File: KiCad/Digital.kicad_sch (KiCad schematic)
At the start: 33 parts, among them IC1 PIC24H, J2 DE9_Plug_MountingHoles, J3 DE9_Plug_MountingHoles, J4 Conn_01x03, J7 Conn_01x05, SW1 SW_DP3T, SW2 SW_DP3T, SW3 SW_DP3T, SW4 OP/CL, SW7 OP/CL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

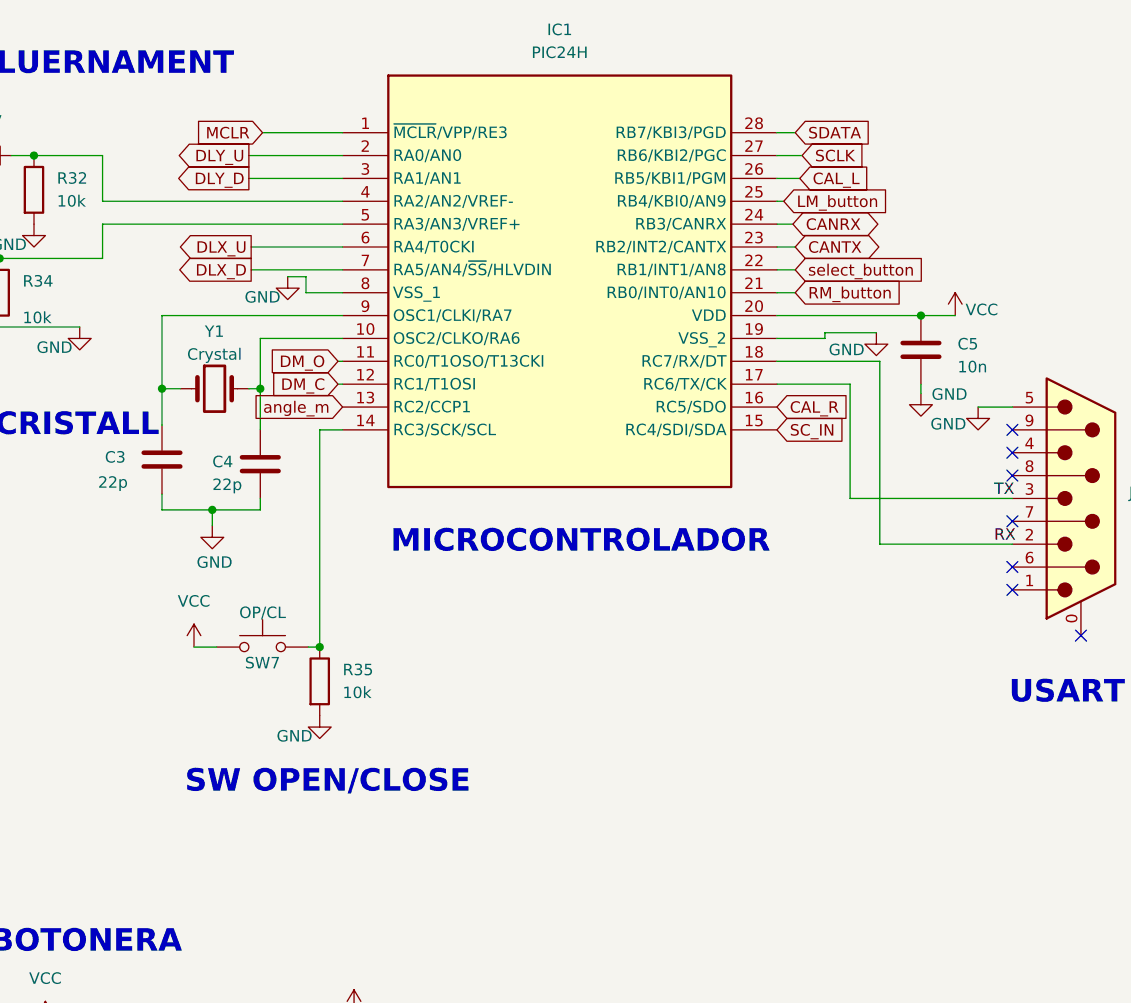
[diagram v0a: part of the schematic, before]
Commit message: afegit esquematic (testpoints + extensor de pines) falta acabar placement
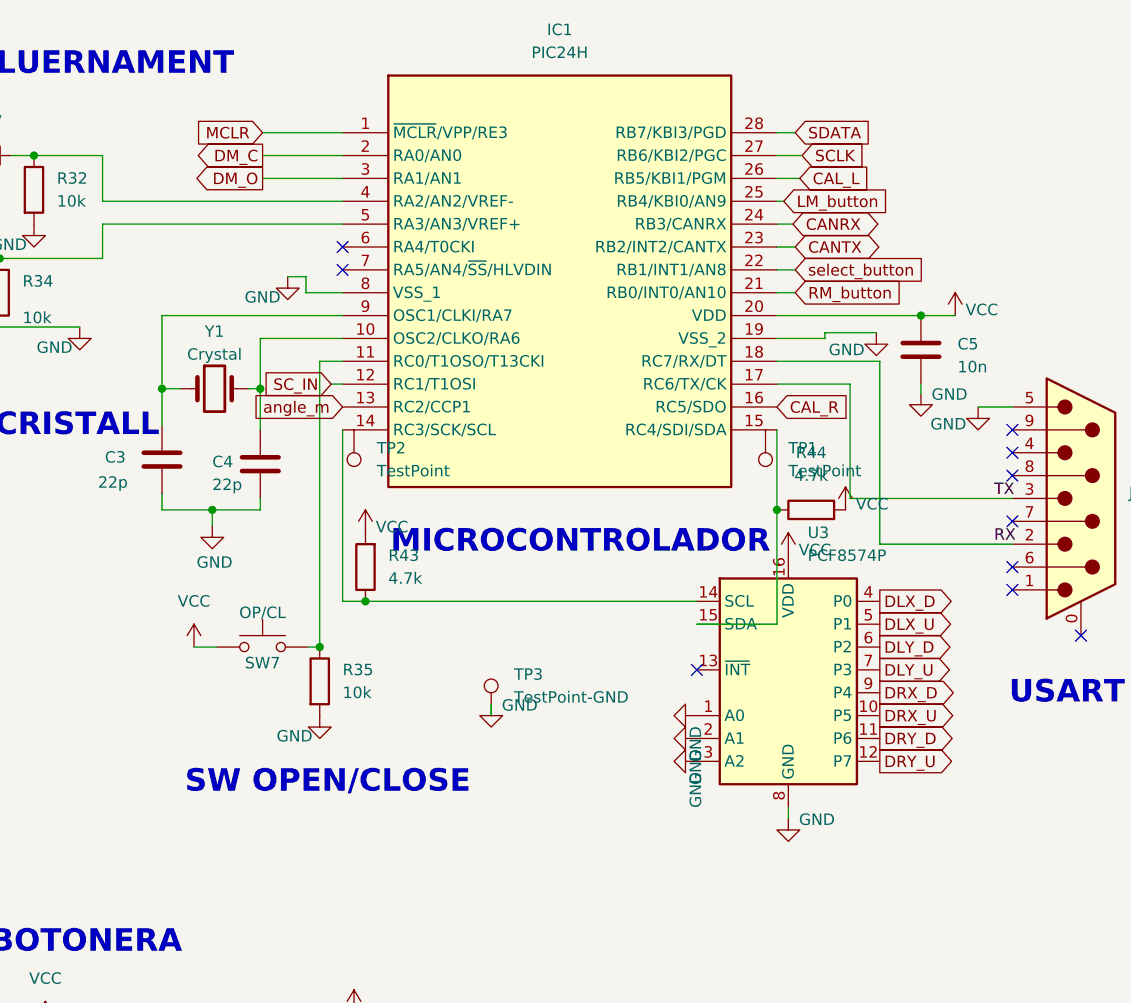
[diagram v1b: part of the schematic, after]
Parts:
- added R43, R44: 4.7k, Resistor_SMD:R_1206_3216Metric_Pad1.30x1.75mm_HandSolder, symbol Device:R
- added TP1, TP2: TestPoint, TestPoint:TestPoint_THTPad_D1.5mm_Drill0.7mm, symbol Connector:TestPoint
- added TP3: TestPoint-GND, TestPoint:TestPoint_THTPad_D1.5mm_Drill0.7mm, symbol Connector:TestPoint
- added U3: PCF8574P, Package_DIP:DIP-16_W7.62mm, symbol Interface_Expansion:PCF8574P
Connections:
- net DLX_D: now also U3.4 (P0); no longer IC1.7 (RA5/AN4/~{SS}/HLVDIN)
- net DLX_U: now also U3.5 (P1); no longer IC1.6 (RA4/T0CKI)
- net DLY_D: now also U3.6 (P2); no longer IC1.3 (RA1/AN1)
- net DLY_U: now also U3.7 (P3); no longer IC1.2 (RA0/AN0)
- net DM_C: now also IC1.2 (RA0/AN0); no longer IC1.12 (RC1/T1OSI)
- net DM_O: now also IC1.3 (RA1/AN1); no longer IC1.11 (RC0/T1OSO/T13CKI)
- net GND: now also TP3.1, U3.1 (A0), U3.2 (A1), U3.3 (A2), U3.8 (GND)
- net SC_IN: now also IC1.12 (RC1/T1OSI); no longer IC1.15 (RC4/SDI/SDA)
- net VCC: now also R43.2, R44.2, U3.16 (VDD)
- net at R35.1, SW7.2: now also IC1.11 (RC0/T1OSO/T13CKI); no longer IC1.14 (RC3/SCK/SCL)
- new net: IC1.14 (RC3/SCK/SCL), R43.1, U3.14 (SCL)
- new net: IC1.15 (RC4/SDI/SDA), R44.1, U3.15 (SDA)
- new net DRX_D: U3.9 (P4)
- new net DRX_U: U3.10 (P5)
- new net DRY_D: U3.11 (P6)
- new net DRY_U: U3.12 (P7)
- no-connect marks 15 -> 18

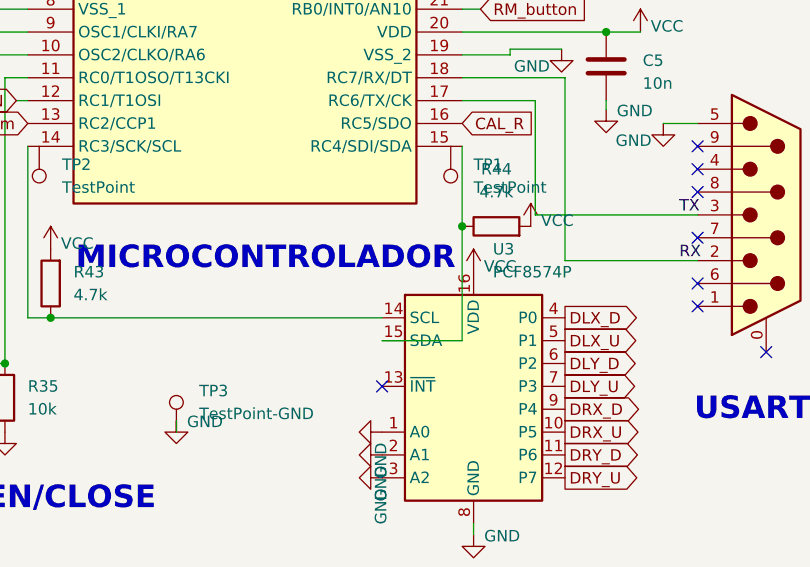
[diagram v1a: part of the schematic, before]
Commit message: canvis placement, afegir els r4emplazos que hi han a la pcb
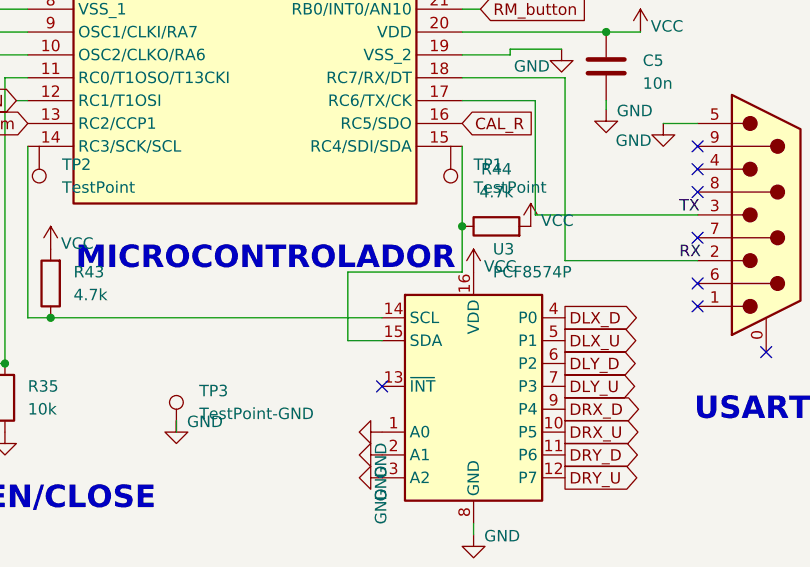
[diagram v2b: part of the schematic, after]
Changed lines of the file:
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@@
+	)
+	(junction
+		(at 132.08 69.85)
+		(diameter 0)
+		(color 0 0 0 0)
 	)
 	(junction
@@
 	)
 	(junction
-		(at 132.08 69.85)
-		(diameter 0)
-		(color 0 0 0 0)
-	)
-	(junction
 		(at 29.21 138.43)
 		(diameter 0)
@@
 	(wire
 		(pts
+			(xy 132.08 74.93) (xy 119.38 74.93)
+		)
+		(stroke
+			(width 0)
+			(type default)
+		)
+	)
+	(wire
+		(pts
+			(xy 119.38 74.93) (xy 119.38 82.55)
+		)
+		(stroke
+			(width 0)
+			(type default)
+		)
+	)
+	(wire
+		(pts
 			(xy 236.474 41.656) (xy 230.378 41.656)
 		)
@@
 	(wire
 		(pts
+			(xy 132.08 69.85) (xy 132.08 74.93)
+		)
+		(stroke
+			(width 0)
+			(type default)
+		)
+	)
+	(wire
+		(pts
 			(xy 198.882 35.56) (xy 201.93 35.56)
 		)
@@
 	(wire
 		(pts
+			(xy 119.38 82.55) (xy 123.19 82.55)
+		)
+		(stroke
+			(width 0)
+			(type default)
+		)
+	)
+	(wire
+		(pts
 			(xy 91.44 135.89) (xy 91.44 134.62)
 		)
@@
 	(wire
 		(pts
-			(xy 123.19 82.55) (xy 132.08 82.55)
-		)
-		(stroke
-			(width 0)
-			(type default)
-		)
-	)
-	(wire
-		(pts
 			(xy 40.64 144.78) (xy 50.8 144.78)
 		)
@@
 		)
 		(stroke
-			(width 0)
-			(type default)
-		)
-	)
-	(wire
-		(pts
-			(xy 132.08 82.55) (xy 132.08 69.85)
-		)
-		(stroke

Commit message: correcions de pcb
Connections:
- net CAL_L: now also IC1.2 (RA0/AN0); no longer IC1.26 (RB5/KBI1/PGM)
- net CAL_R: now also IC1.3 (RA1/AN1); no longer IC1.16 (RC5/SDO)
- net DLX_D: now also U3.9 (P4); no longer U3.4 (P0)
- net DLX_U: now also U3.10 (P5); no longer U3.5 (P1)
- net DLY_D: now also U3.4 (P0); no longer U3.6 (P2)
- net DLY_U: now also U3.5 (P1); no longer U3.7 (P3)
- net DM_C: now also U3.7 (P3); no longer IC1.2 (RA0/AN0)
- net DM_O: now also U3.6 (P2); no longer IC1.3 (RA1/AN1)
- net DRX_D: now also U3.11 (P6); no longer U3.9 (P4)
- net DRX_U: now also U3.12 (P7); no longer U3.10 (P5)
- net DRY_D: now also IC1.6 (RA4/T0CKI); no longer U3.11 (P6)
- net DRY_U: now also IC1.7 (RA5/AN4/~{SS}/HLVDIN); no longer U3.12 (P7)
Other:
- moved on the sheet: R31, R32, R33, R34

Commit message: pcb Tota connectada
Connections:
- net DLX_D: now also U3.12 (P7); no longer U3.9 (P4)
- net DRX_U: now also U3.9 (P4); no longer U3.12 (P7)
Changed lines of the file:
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@@
+		)
+	)
+	(global_label "DRX_U"
+		(shape output)
+		(at 143.51 90.17 0)
+		(fields_autoplaced yes)
+		(effects
+			(font
+				(size 1.27 1.27)
+			)
+			(justify left)
+		)
+		(property "Intersheetrefs" "${INTERSHEET_REFS}"
+			(at 152.5428 90.17 0)
+			(effects
+				(font
+					(size 1.27 1.27)
+				)
+				(justify left)
+				(hide yes)
+			)
 		)
 	)
@@
 		)
 	)
+	(global_label "DLX_D"
+		(shape output)
+		(at 143.51 97.79 0)
+		(fields_autoplaced yes)
+		(effects
+			(font
+				(size 1.27 1.27)
+			)
+			(justify left)
+		)
+		(property "Intersheetrefs" "${INTERSHEET_REFS}"
+			(at 152.2404 97.79 0)
+			(effects
+				(font
+					(size 1.27 1.27)
+				)
+				(justify left)
+				(hide yes)
+			)
+		)
+	)
 	(global_label "CAL_L"
 		(shape input)
@@
 		)
 	)
-	(global_label "DLX_D"
-		(shape output)
-		(at 143.51 90.17 0)
-		(fields_autoplaced yes)
-		(effects
-			(font
-				(size 1.27 1.27)
-			)
-			(justify left)
-		)
-		(property "Intersheetrefs" "${INTERSHEET_REFS}"
-			(at 152.2404 90.17 0)
-			(effects
-				(font
-					(size 1.27 1.27)
-				)
-				(justify left)
-				(hide yes)
-			)
-		)
-	)
 	(global_label "DRY_D"
 		(shape output)
@@
 			(effects
 				(font
-					(size 1.27 1.27)
-				)
-				(justify left)
-				(hide yes)
-			)
-		)
-	)
-	(global_label "DRX_U"
-		(shape output)
-		(at 143.51 97.79 0)
-		(fields_autoplaced yes)
-		(effects
-			(font
-				(size 1.27 1.27)
-			)
-			(justify left)
-		)
-		(property "Intersheetrefs" "${INTERSHEET_REFS}"
-			(at 152.5428 97.79 0)
-			(effects
-				(font

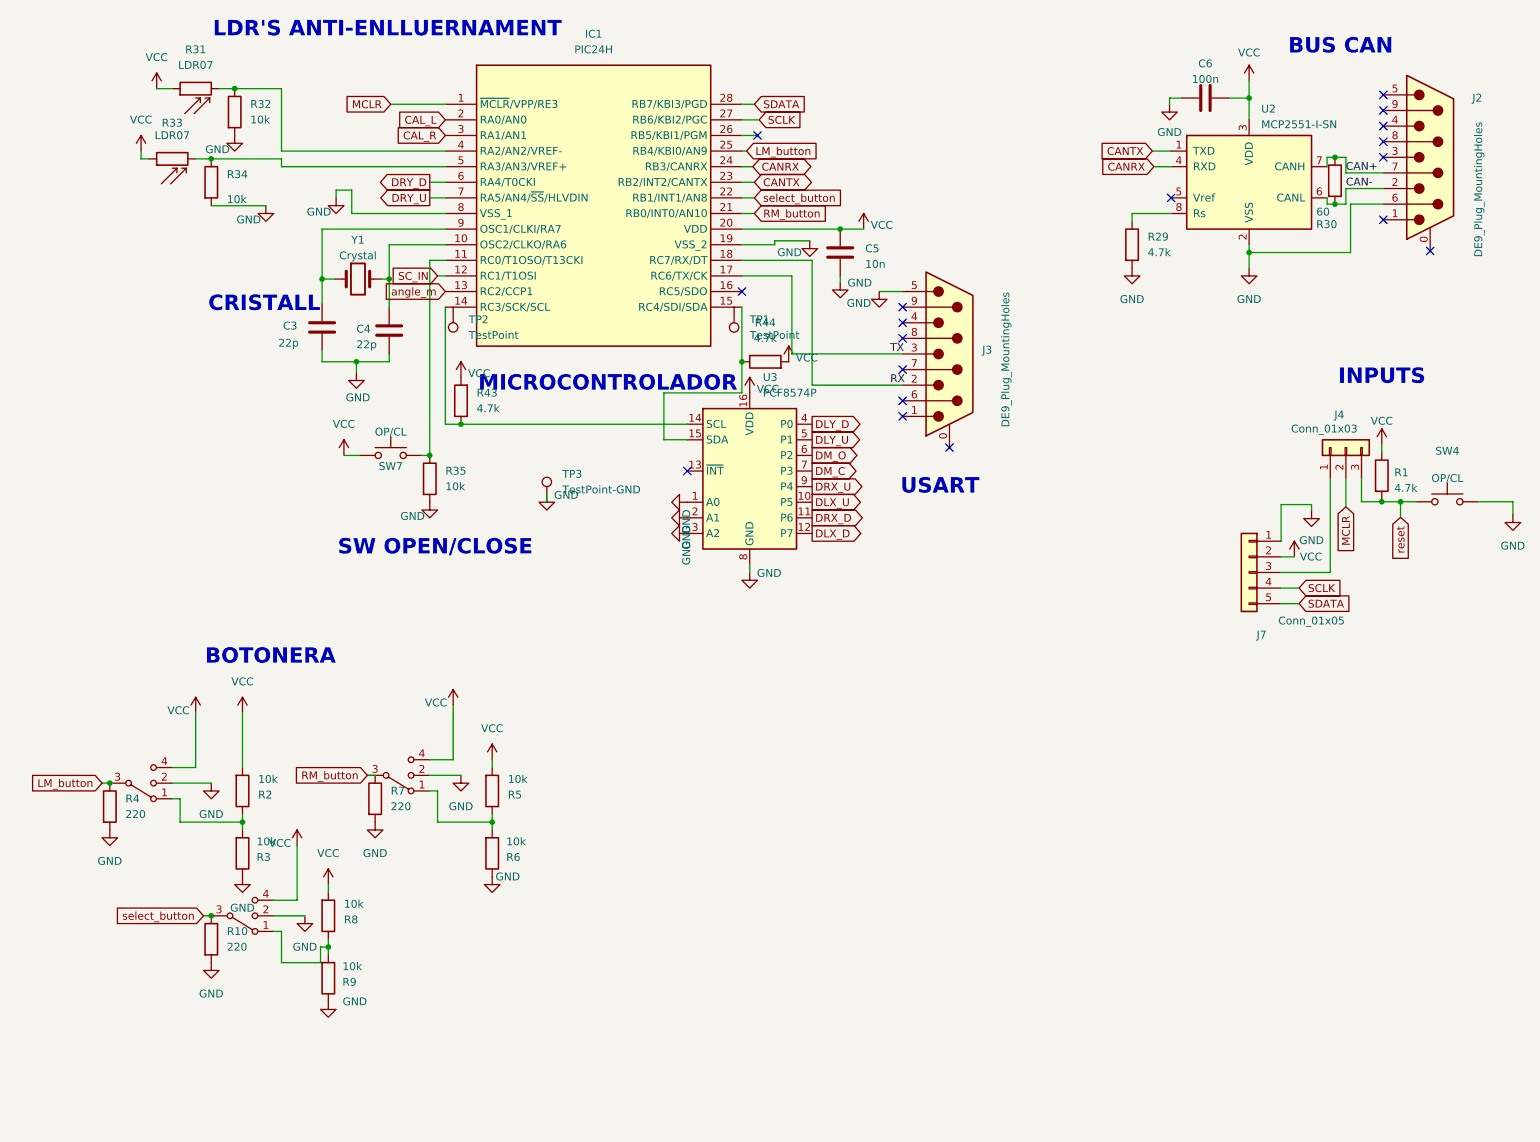
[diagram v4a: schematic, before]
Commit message: final de pcb, falta els test points
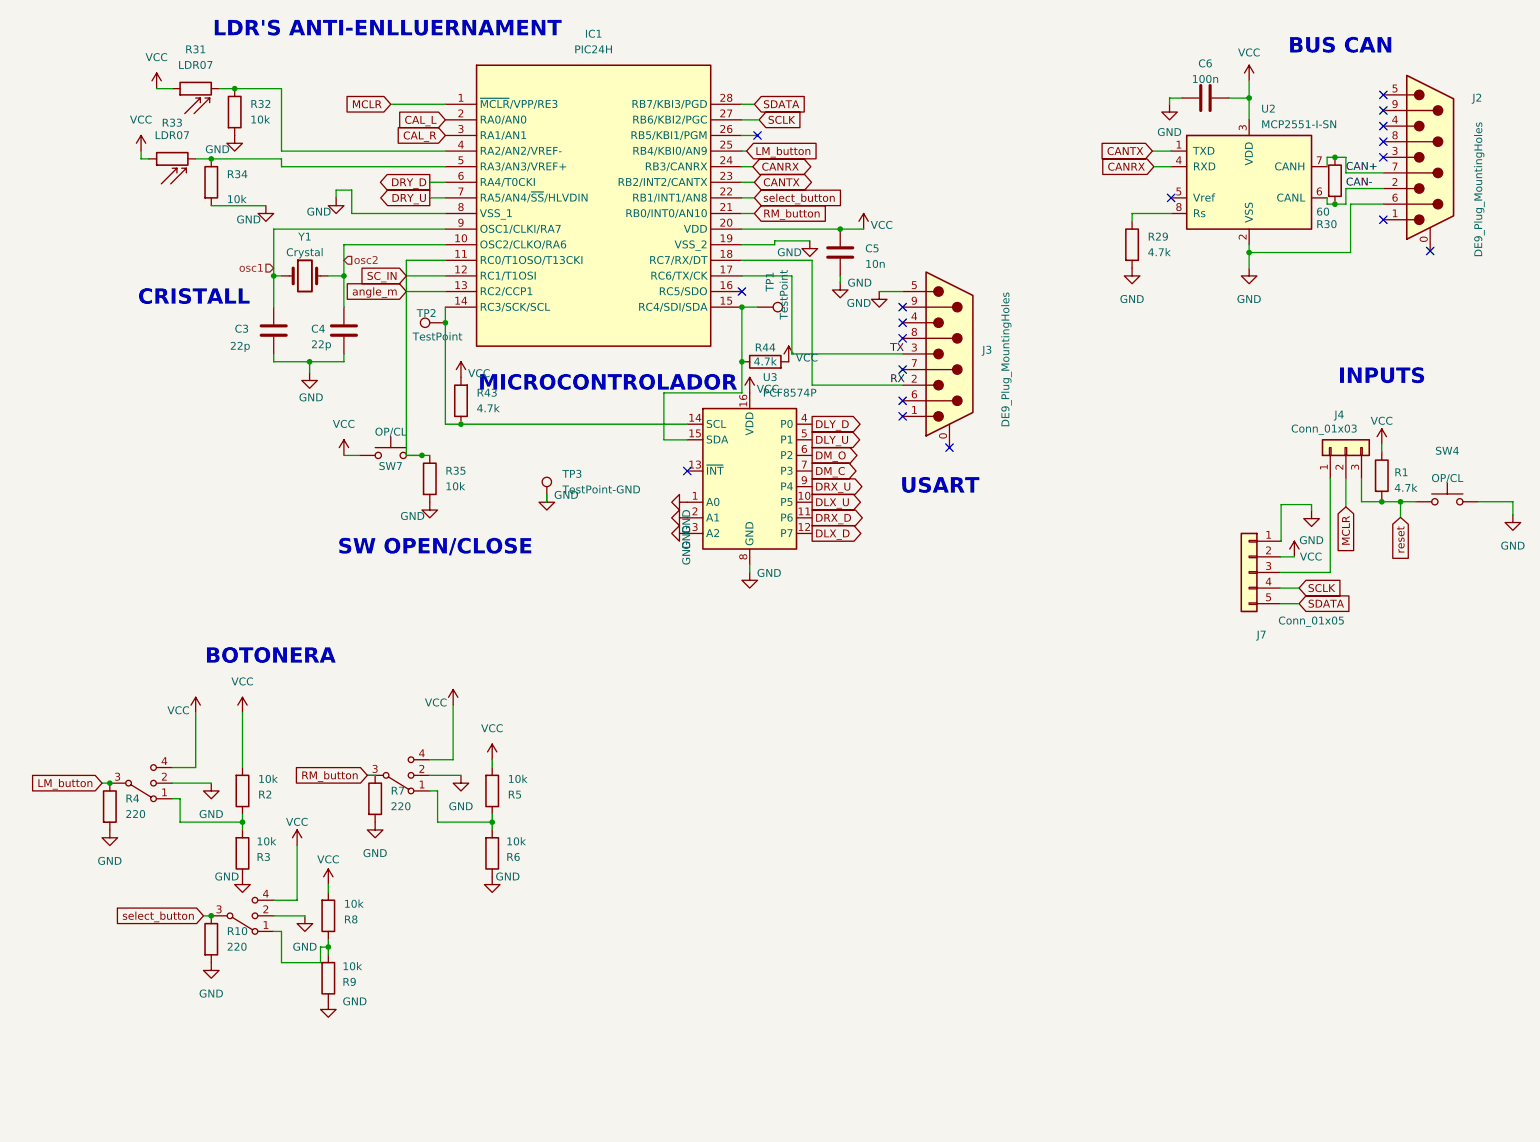
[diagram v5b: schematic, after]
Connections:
- net angle_m is gone; now on net SC_IN: IC1.13 (RC2/CCP1)
- net SC_IN: now also IC1.11 (RC0/T1OSO/T13CKI), R35.1, SW7.2
- net osc2: now reaches C4.1, IC1.10 (OSC2/CLKO/RA6), Y1.2
- net at IC1.14 (RC3/SCK/SCL), R43.1, U3.14 (SCL): now also TP2.1
- net at IC1.15 (RC4/SDI/SDA), R44.1, U3.15 (SDA): now also TP1.1
- net osc1: now reaches C3.1, IC1.9 (OSC1/CLKI/RA7), Y1.1
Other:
- moved on the sheet: C3, C4, TP1, TP2, Y1

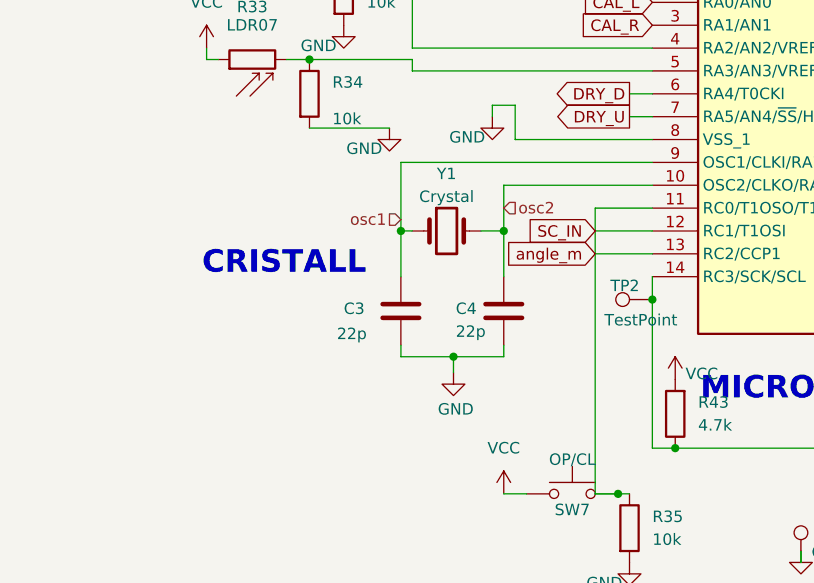
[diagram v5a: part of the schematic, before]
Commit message: petites modificacions resistencies part digital + resolucio errors pcb
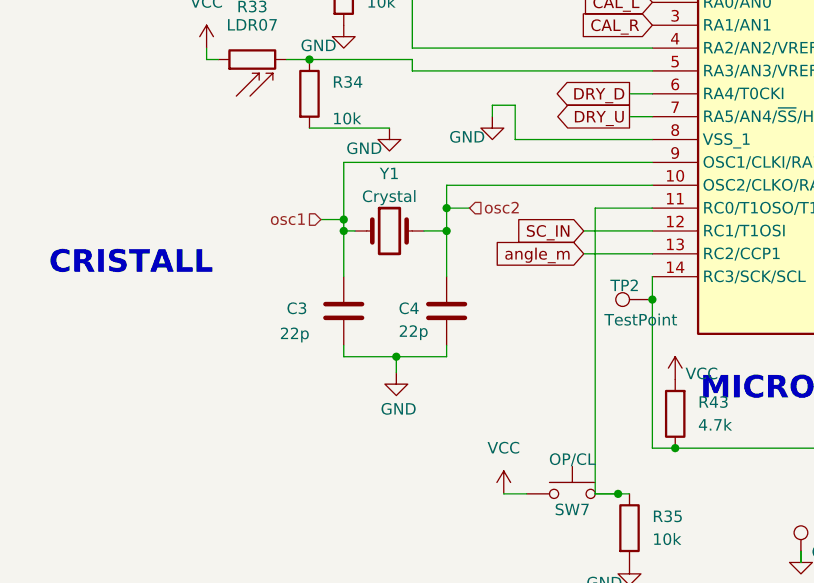
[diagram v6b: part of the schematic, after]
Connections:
- net SC_IN: no longer IC1.11 (RC0/T1OSO/T13CKI), IC1.13 (RC2/CCP1), R35.1, SW7.2
- new net: IC1.11 (RC0/T1OSO/T13CKI), R35.1, SW7.2
- new net angle_m: IC1.13 (RC2/CCP1)
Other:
- moved on the sheet: C3, C4, Y1

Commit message: canvis pcb finals
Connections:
- net CAL_L: now also IC1.5 (RA3/AN3/VREF+); no longer IC1.2 (RA0/AN0)
- net CAL_R: now also IC1.4 (RA2/AN2/VREF-); no longer IC1.3 (RA1/AN1)
- net CANRX: now also IC1.23 (RB3/CANRX); no longer IC1.24 (RB3/CANRX)
- net CANTX: now also IC1.24 (RB2/INT2/CANTX); no longer IC1.23 (RB2/INT2/CANTX)
- net DLY_U: now also U3.6 (P2); no longer U3.5 (P1)
- net DM_C: now also U3.5 (P1); no longer U3.7 (P3)
- net DM_O: now also U3.7 (P3); no longer U3.6 (P2)
- net MCLR: now also J4.3 (Pin_3); no longer J4.2 (Pin_2)
- net SC_IN: now also IC1.16 (RC5/SDO); no longer IC1.12 (RC1/T1OSI)
- net reset: now also J4.2 (Pin_2); no longer J4.3 (Pin_3)
- net at R31.2, R32.1: now also IC1.2 (RA0/AN0); no longer IC1.4 (RA2/AN2/VREF-)
- net at R33.2, R34.1: now also IC1.3 (RA1/AN1); no longer IC1.5 (RA3/AN3/VREF+)
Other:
- moved on the sheet: J4, R1, SW4
